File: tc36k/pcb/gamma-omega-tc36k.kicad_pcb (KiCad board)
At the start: 2 copper layers, 232.8 x 111.4 mm, 45 parts

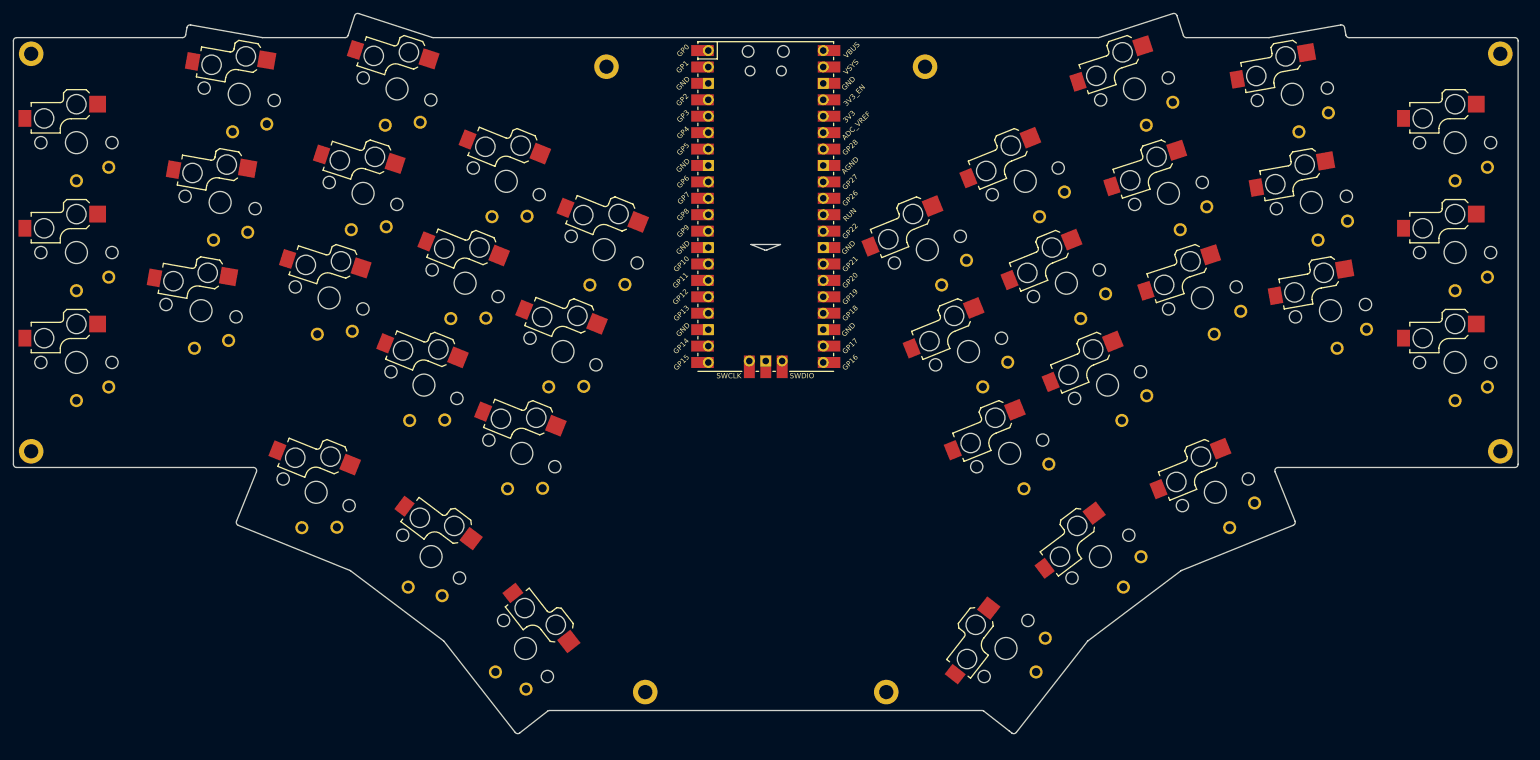
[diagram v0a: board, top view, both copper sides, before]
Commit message: Adding hotswap/soldering traces and core column traces
A few of the left-hand traces are deliberately different to allow
adding a scan-row trace on the same side.
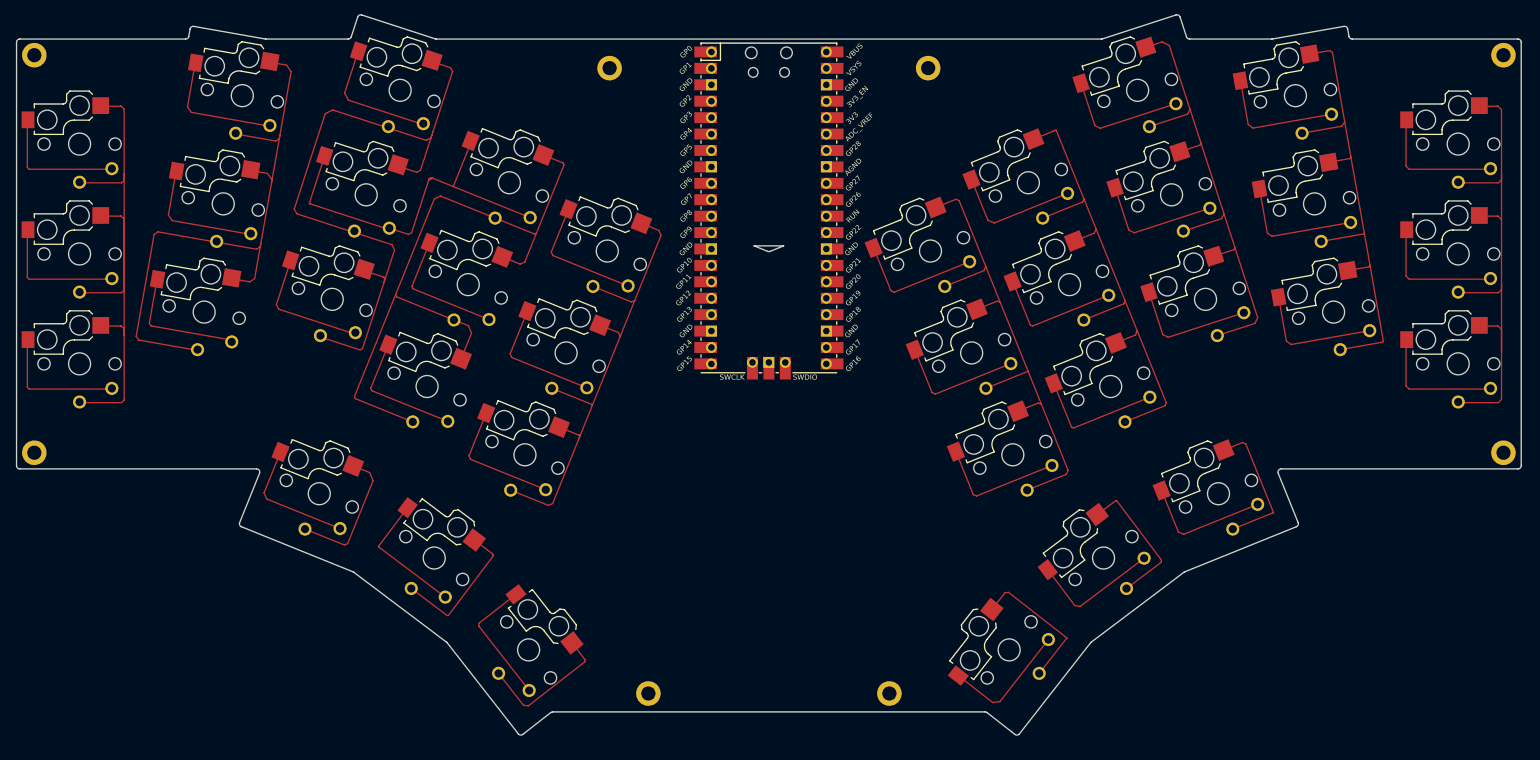
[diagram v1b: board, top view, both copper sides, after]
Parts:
- moved S9 0.53 mm to (100.1, 57.9)
- moved S32 0.53 mm to (188.5, 98.5)
- moved H1 0.53 mm to (43.5, 52.5)
- moved S13 0.53 mm to (119.4, 114.3)
- moved S35 0.53 mm to (208.9, 130.3)
- moved S6 0.53 mm to (75.7, 58.7)
- moved S16 0.53 mm to (87.6, 120.3)
- moved S30 0.53 mm to (197.3, 72.2)
- moved H2 0.53 mm to (270.8, 52.5)
- moved S12 0.53 mm to (117.0, 72.2)
- moved S27 0.53 mm to (214.2, 57.9)
- moved S7 0.53 mm to (89.6, 90.2)
- moved S19 0.53 mm to (263.8, 100.2)
- moved H5 0.53 mm to (132.5, 54.5)
- moved S33 0.53 mm to (182.1, 82.8)
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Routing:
- net C4: track 0.00 -> 101.5 mm
- net C3: track 0.00 -> 101.2 mm
- net C2: track 0.00 -> 95.6 mm
- net C1: track 0.00 -> 91.4 mm
- net C12: track 0.00 -> 82.4 mm
- net C7: track 0.00 -> 78.7 mm
- net C6: track 0.00 -> 78.2 mm
- net R4: track 0.00 -> 78.1 mm
- net C5: track 0.00 -> 77.0 mm
- net C10: track 0.00 -> 77.0 mm
- net C8: track 0.00 -> 76.6 mm
- net R13: track 0.00 -> 60.9 mm
- net R9: track 0.00 -> 60.9 mm
- net R7: track 0.00 -> 60.7 mm
- net R2: track 0.00 -> 60.7 mm
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
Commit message: Front traces in KiCad
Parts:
- moved S3 1.49 mm to (50.2, 67.7)
- moved S18 1.49 mm to (119.7, 145.9)
- moved S1 1.49 mm to (50.2, 101.7)
- moved S25 1.49 mm to (224.4, 91.7)
- moved S16 1.49 mm to (87.3, 121.8)
- moved S34 1.49 mm to (226.4, 121.8)
- moved S21 1.49 mm to (263.5, 67.7)
- moved S15 1.49 mm to (131.8, 84.2)
- moved H5 1.49 mm to (132.2, 55.9)
- moved S33 1.49 mm to (181.8, 84.2)
- moved S4 1.49 mm to (69.5, 93.7)
- moved S26 1.49 mm to (219.1, 75.5)
- moved S36 1.49 mm to (194.0, 145.9)
- moved S13 1.49 mm to (119.1, 115.8)
- moved H2 1.49 mm to (270.5, 53.9)
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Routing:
- net R7: track 60.7 -> 224.5 mm
- net R1: track 40.8 -> 188.0 mm
- net C13: track 44.0 -> 188.9 mm
- net R13: track 60.9 -> 202.9 mm
- net C12: track 82.4 -> 221.6 mm
- net R3: track 40.3 -> 166.4 mm
- net C2: track 95.6 -> 219.7 mm
- net C1: track 91.4 -> 213.8 mm
- net C10: track 77.0 -> 199.1 mm
- net C11: track 44.3 -> 143.3 mm
- net C9: track 44.3 -> 118.6 mm
- net R5: track 40.6 -> 102.5 mm
- net C8: track 76.6 -> 133.4 mm
- net C3: track 101.2 -> 143.2 mm
- net C7: track 78.7 -> 118.8 mm
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
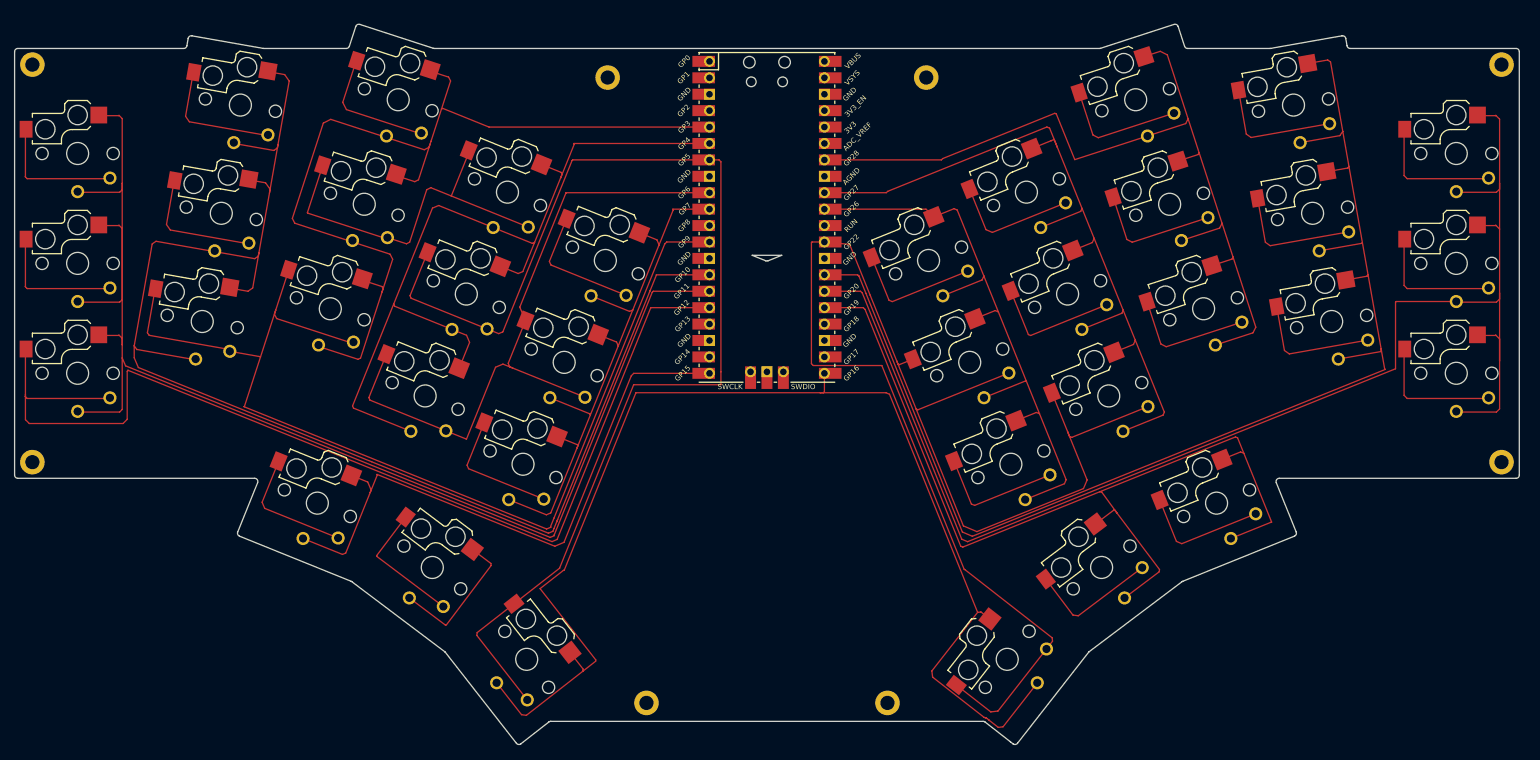
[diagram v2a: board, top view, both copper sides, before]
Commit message: Back traces in KiCad
The R6 trace to column C6 is making lots of row detours.
This wasn't very obvious on my paper sketch.
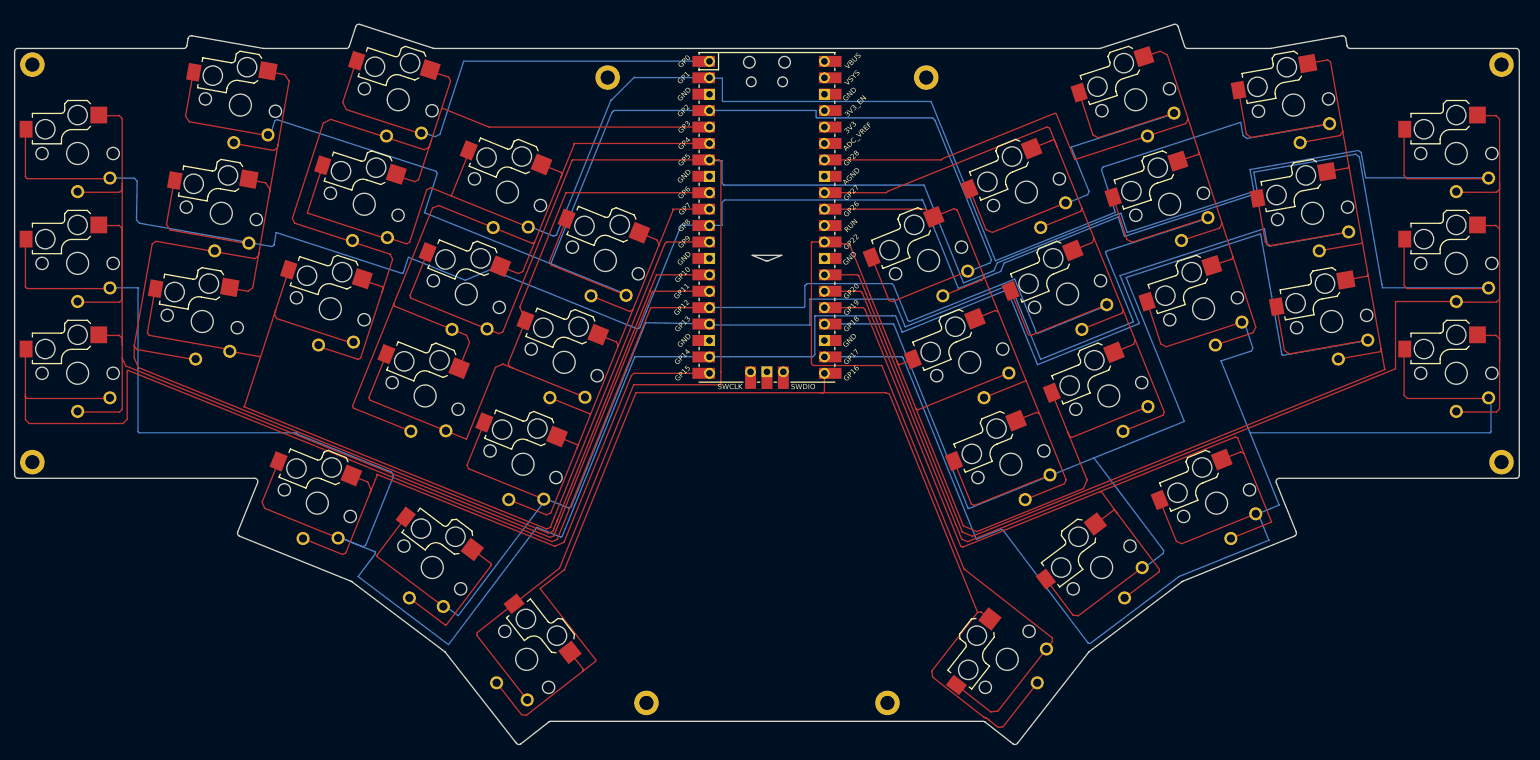
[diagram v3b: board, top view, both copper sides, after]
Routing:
- net R10: track 60.6 -> 372.2 mm
- net R2: track 60.7 -> 339.2 mm
- net R12: track 60.5 -> 245.9 mm
- net R9: track 60.9 -> 242.2 mm
- net R11: track 60.6 -> 238.5 mm
- net R6: track 60.7 -> 235.2 mm
- net R4: track 77.4 -> 251.4 mm
- net R13: track 202.9 -> 350.8 mm
- net R8: track 60.2 -> 141.5 mm
- net R1: track 188.0 -> 264.5 mm

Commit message: Move R6/C6 trace from back to front
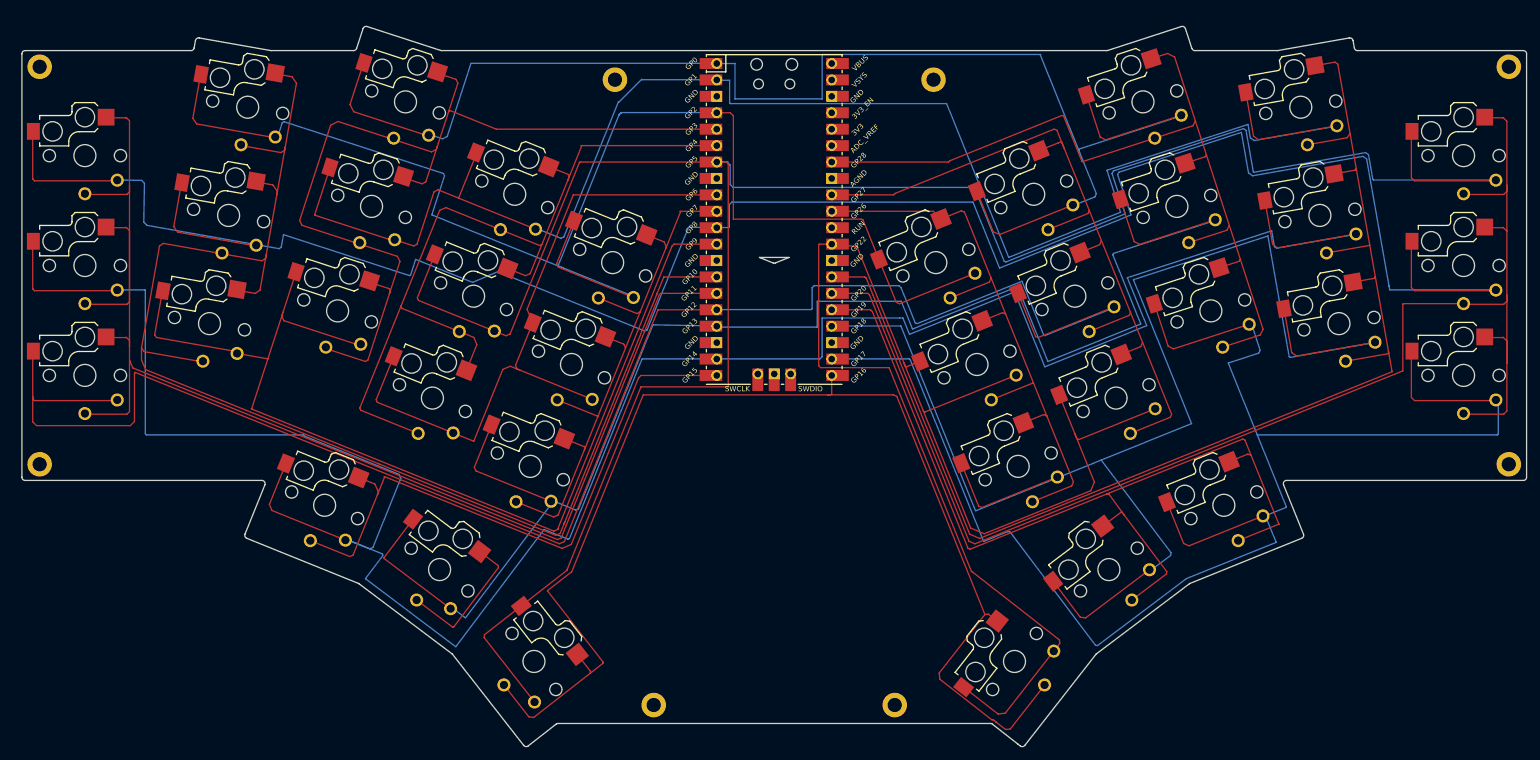
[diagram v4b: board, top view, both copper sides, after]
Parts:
- moved S32 1.17 mm to (189.3, 100.3)
- moved S15 1.17 mm to (133.0, 84.6)
- moved S36 1.17 mm to (195.1, 146.3)
- moved H4 1.17 mm to (271.6, 115.8)
- moved S1 1.17 mm to (51.3, 102.0)
- moved H1 1.17 mm to (44.3, 54.3)
- moved S24 1.17 mm to (239.4, 60.5)
- moved S18 1.17 mm to (120.8, 146.3)
- moved H6 1.17 mm to (182.6, 56.3)
- moved S30 1.17 mm to (198.1, 74.0)
- moved H2 1.17 mm to (271.6, 54.3)
- moved S34 1.17 mm to (227.5, 122.1)
- moved H8 1.17 mm to (176.6, 153.0)
- moved S10 1.17 mm to (105.1, 105.5)
- moved _1 1.17 mm to (158.0, 77.9)
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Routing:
- net R8: track 141.5 -> 220.1 mm
- net R6: track 235.2 -> 217.8 mm
- net R13: track 350.8 -> 358.8 mm
- net R2: track 339.2 -> 343.7 mm
- net R4: track 251.4 -> 250.4 mm

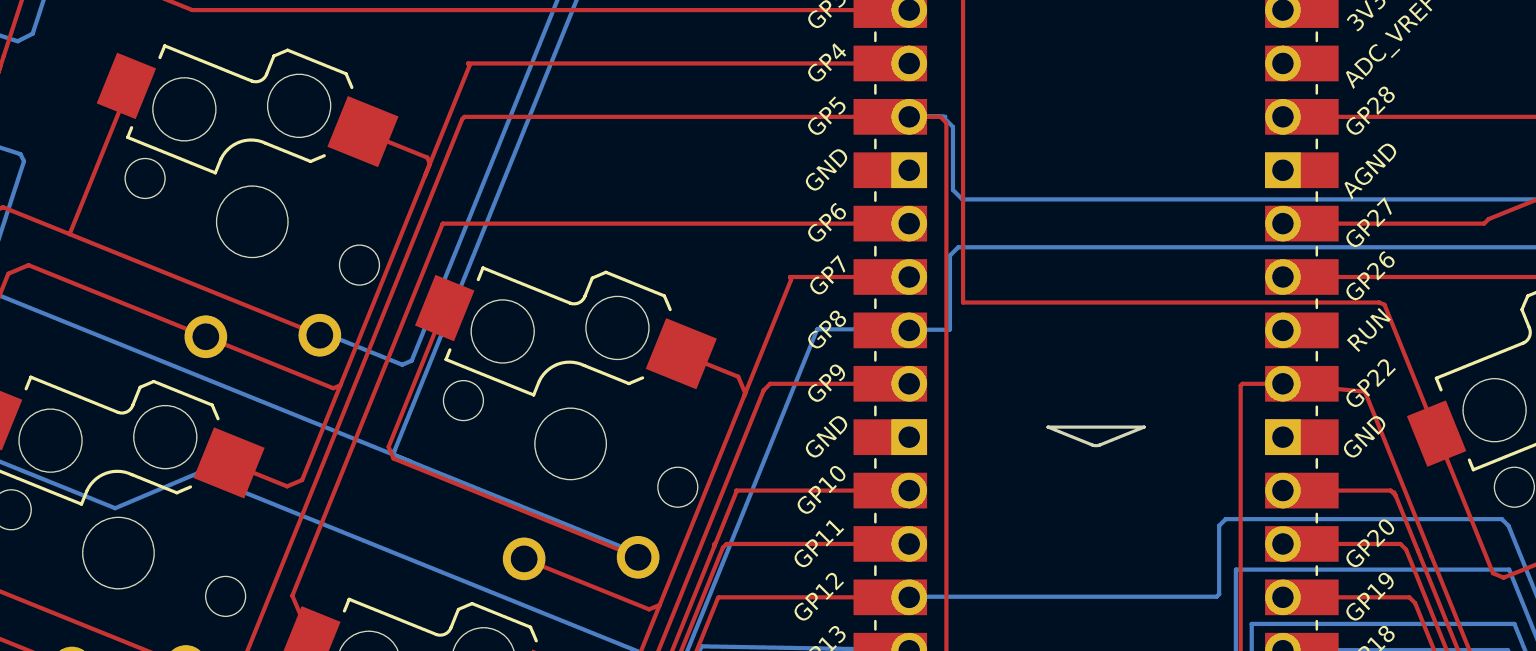
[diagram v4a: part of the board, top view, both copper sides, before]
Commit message: Restore missing GP21 silkscreen label
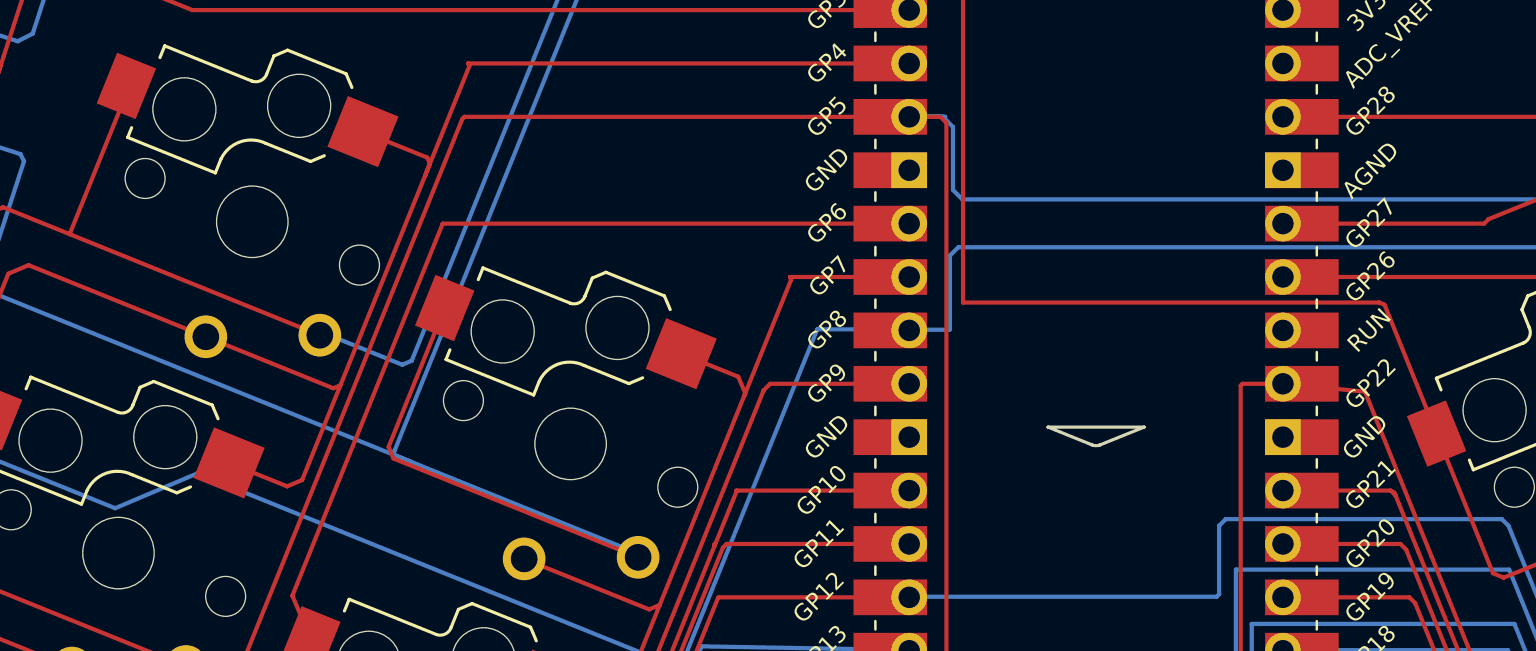
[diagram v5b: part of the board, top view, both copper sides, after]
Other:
- board text added: "GP21"
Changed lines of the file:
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@@
 		(attr exclude_from_pos_files exclude_from_bom allow_soldermask_bridges)
 		(fp_line
-			(start -6.999997 -1.499991)
+			(start -6.999997 -1.49999)
 			(end -7 -2)
 			(stroke
@@
 		(fp_line
 			(start -2.5 -1.5)
-			(end -6.999997 -1.499991)
+			(end -6.999997 -1.49999)
 			(stroke
 				(width 0.15)
@@
 		(attr exclude_from_pos_files exclude_from_bom allow_soldermask_bridges)
 		(fp_line
-			(start -6.999997 -1.499991)
+			(start -6.999997 -1.49999)
 			(end -7 -2)
 			(stroke
@@
 		(fp_line
 			(start -2.5 -1.5)
-			(end -6.999997 -1.499991)
+			(end -6.999997 -1.49999)
 			(stroke
 				(width 0.15)
@@
 		)
 		(pad "" np_thru_hole circle
-			(at 0.000004 -5.950011 342)
+			(at 0.000004 -5.95001 342)
 			(size 3 3)
 			(drill 3)
@@
 		(attr exclude_from_pos_files exclude_from_bom allow_soldermask_bridges)
 		(fp_line
-			(start -6.999997 -1.499991)
+			(start -6.999997 -1.49999)
 			(end -7 -2)
 			(stroke
@@
 		(fp_line
 			(start -2.5 -1.5)
-			(end -6.999997 -1.499991)
+			(end -6.999997 -1.49999)
 			(stroke
 				(width 0.15)
@@
 		)
 		(pad "" np_thru_hole circle
-			(at 0.000004 -5.950011 342)
+			(at 0.000004 -5.95001 342)
 			(size 3 3)
 			(drill 3)
@@
 		(attr exclude_from_pos_files exclude_from_bom allow_soldermask_bridges)
 		(fp_line
-			(start -6.999997 -1.499991)
+			(start -6.999997 -1.49999)
 			(end -7 -2)
 			(stroke
@@
 		(fp_line
 			(start -2.5 -1.5)
-			(end -6.999997 -1.499991)
+			(end -6.999997 -1.49999)
 			(stroke
 				(width 0.15)
@@
 		(attr exclude_from_pos_files exclude_from_bom allow_soldermask_bridges)
 		(fp_line
-			(start -6.999997 -1.499991)
+			(start -6.999997 -1.49999)
 			(end -7 -2)
 			(stroke
@@
 		(fp_line
 			(start -2.5 -1.5)
-			(end -6.999997 -1.499991)
+			(end -6.999997 -1.49999)
 			(stroke
 				(width 0.15)
@@
 		(attr exclude_from_pos_files exclude_from_bom allow_soldermask_bridges)
 		(fp_line
-			(start -6.999997 -1.499991)
+			(start -6.999997 -1.49999)
 			(end -7 -2)
 			(stroke
@@
 		(fp_line
 			(start -2.5 -1.5)
-			(end -6.999997 -1.499991)
+			(end -6.999997 -1.49999)
 			(stroke
 				(width 0.15)
@@
 		)
 		(pad "" np_thru_hole circle
-			(at 0.000004 -5.950011 342)
+			(at 0.000004 -5.95001 342)
 			(size 3 3)
 			(drill 3)
@@
 		(attr exclude_from_pos_files exclude_from_bom allow_soldermask_bridges)
 		(fp_line
-			(start -6.999997 -1.499991)
+			(start -6.999997 -1.49999)
 			(end -7 -2)
 			(stroke
@@
 		(fp_line
 			(start -2.5 -1.5)
-			(end -6.999997 -1.499991)
+			(end -6.999997 -1.49999)
 			(stroke
 				(width 0.15)
@@
 		(layer "Edge.Cuts")
 	)
+	(gr_text "GP21"
+		(at 171 86.5 45)
+		(layer "F.SilkS")
+		(effects
+			(font
+				(size 0.8 0.8)
+				(thickness 0.15)
+			)
+		)
+	)
 	(segment
